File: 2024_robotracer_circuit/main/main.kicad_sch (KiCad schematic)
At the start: 71 parts, among them J1 PH_6p, J10 PH_5p, J11 PH_6p, J12 PH_4p, J13 PH_8p, J14 PH_6p, J2 Conn_02x05_Odd_Even, J3 Conn_02x05_Odd_Even, J4 PA_2p, J5 PA_2p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

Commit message: LEDつながた
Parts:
- removed J12: PH_4p, Connector_JST:JST_PH_B4B-PH-K_1x04_P2.00mm_Vertical, symbol Connector_Generic:Conn_01x04
- removed J14: PH_6p, Connector_JST:JST_PH_B6B-PH-K_1x06_P2.00mm_Vertical, symbol Connector_Generic:Conn_01x06
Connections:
- net ENC1_A: now also U1.37 (PC6); no longer U1.58 (PB6)
- net ENC1_B: now also U1.38 (PC7); no longer U1.59 (PB7)
- net ENC2_A: now also U1.58 (PB6); no longer U1.38 (PC7)
- net ENC2_B: now also U1.59 (PB7); no longer U1.37 (PC6)
- net LCD_SCL: now also J8.3 (Pin_3), R35.2; no longer J8.2 (Pin_2), R34.2
- net LCD_SDA: now also J8.2 (Pin_2), R34.2; no longer J8.3 (Pin_3), R35.2
- net LED0: now also U1.45 (PA12); no longer U1.8 (PC0)
- net LED1: now also U1.56 (PB4); no longer U1.9 (PC1)
- net LED2: now also U1.57 (PB5); no longer U1.2 (PC13)
- net LED3: now also U1.2 (PC13); no longer U1.3 (PC14)
- net LED4: now also U1.3 (PC14); no longer U1.4 (PC15)
- net LED5: now also U1.4 (PC15); no longer U1.33 (PB12)
- net LED6: now also U1.8 (PC0); no longer U1.57 (PB5)
- net LED7: now also U1.9 (PC1); no longer U1.56 (PB4)
- net LED9: now also U1.33 (PB12); no longer U1.45 (PA12)
- net MOTOR1_IN_A: now also U1.42 (PA9); no longer U1.41 (PA8)
- net MOTOR1_IN_B: now also U1.41 (PA8); no longer U1.42 (PA9)
- net MOTOR2_IN_A: now also U1.44 (PA11); no longer U1.43 (PA10)
- net MOTOR2_IN_B: now also U1.43 (PA10); no longer U1.44 (PA11)
- net SENSOR0_ADC: now also U1.17 (PA3); no longer U1.14 (PA0)
- net SENSOR1_ADC: now also U1.16 (PA2); no longer U1.15 (PA1)
- net SENSOR2_ADC: now also U1.15 (PA1); no longer U1.16 (PA2)
- net SENSOR3_ADC: now also U1.14 (PA0); no longer U1.17 (PA3)
- net SW_A: now also U1.24 (PC4); no longer U1.23 (PA7)
- net SW_B: now also U1.23 (PA7); no longer U1.24 (PC4)
- net SW_C: now also U1.27 (PB1); no longer U1.26 (PB0)
- net SW_D: now also U1.26 (PB0); no longer U1.27 (PB1)
- net PWM_GP: no longer names the net of U1.36 (PB15)
- net SPI_MISO_GP: no longer names the net of U1.10 (PC2)
- net SPI_MOSI_GP: no longer names the net of U1.11 (PC3)
- net SPI_SCK_GP: no longer names the net of U1.34 (PB13)
- net USART_RX: no longer names the net of U1.52 (PC11)
- net USART_TX: no longer names the net of U1.51 (PC10)
- no-connect marks 18 -> 24

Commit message: 修正
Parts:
- R23: value R_Small -> 1.8k
- R24: value R_Small -> 1k
- U3, U4: footprint Package_SO:TSSOP-8_3x3mm_P0.65mm -> Package_SO:SOP-8_3.9x4.9mm_P1.27mm
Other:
- moved on the sheet: BZ1, D1, J10, J11, J7, J9, R22, R23, R24, R5, R6, R7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

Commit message: hoge
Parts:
- J7: value HX_12p -> XH_12p
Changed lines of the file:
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@@
 			)
 		)
-		(property "Value" "HX_12p"
+		(property "Value" "XH_12p"
 			(at 59.69 154.9399 0)
 			(effects

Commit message: 修正
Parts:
- R31: value R_Small -> 5.1k
- R32: value R_Small -> 1.8k
- R33: value R_Small -> 3k
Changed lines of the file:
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@@
 			)
 		)
-		(property "Value" "R_Small"
+		(property "Value" "1.8k"
 			(at 179.07 41.9099 0)
 			(effects
@@
 			)
 		)
-		(property "Value" "R_Small"
+		(property "Value" "5.1k"
 			(at 90.17 39.3699 0)
 			(effects
@@
 			)
 		)
-		(property "Value" "R_Small"
+		(property "Value" "3k"
 			(at 175.26 73.6599 0)
 			(effects

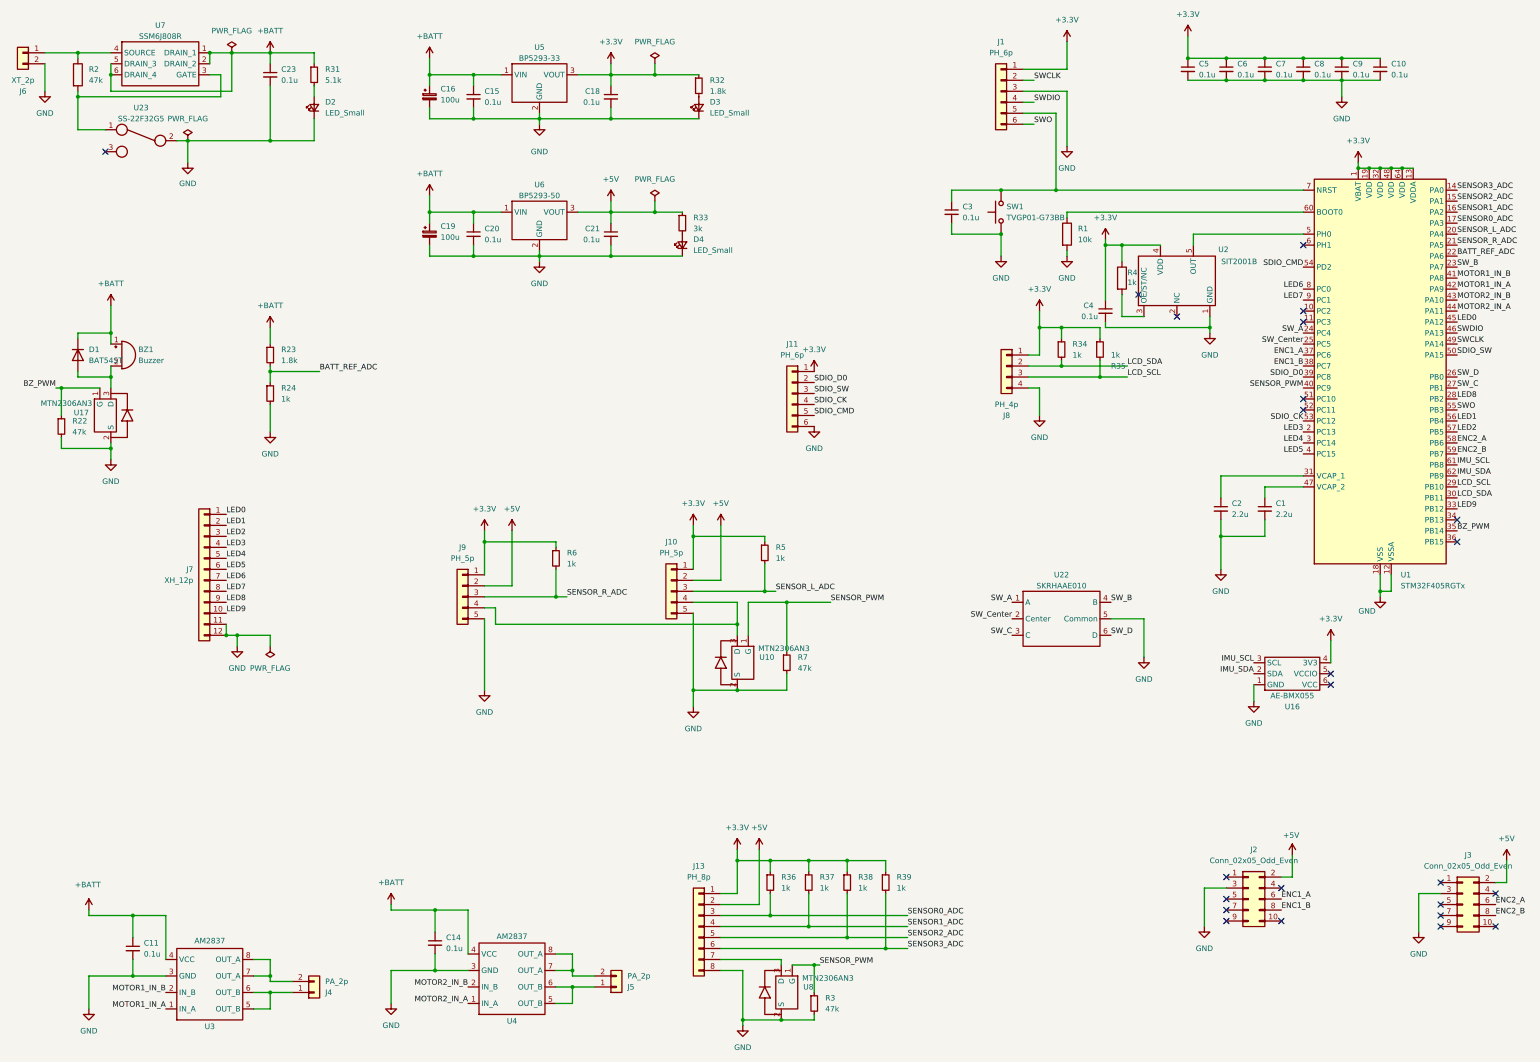
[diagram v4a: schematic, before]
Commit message: 回路を大幅修正
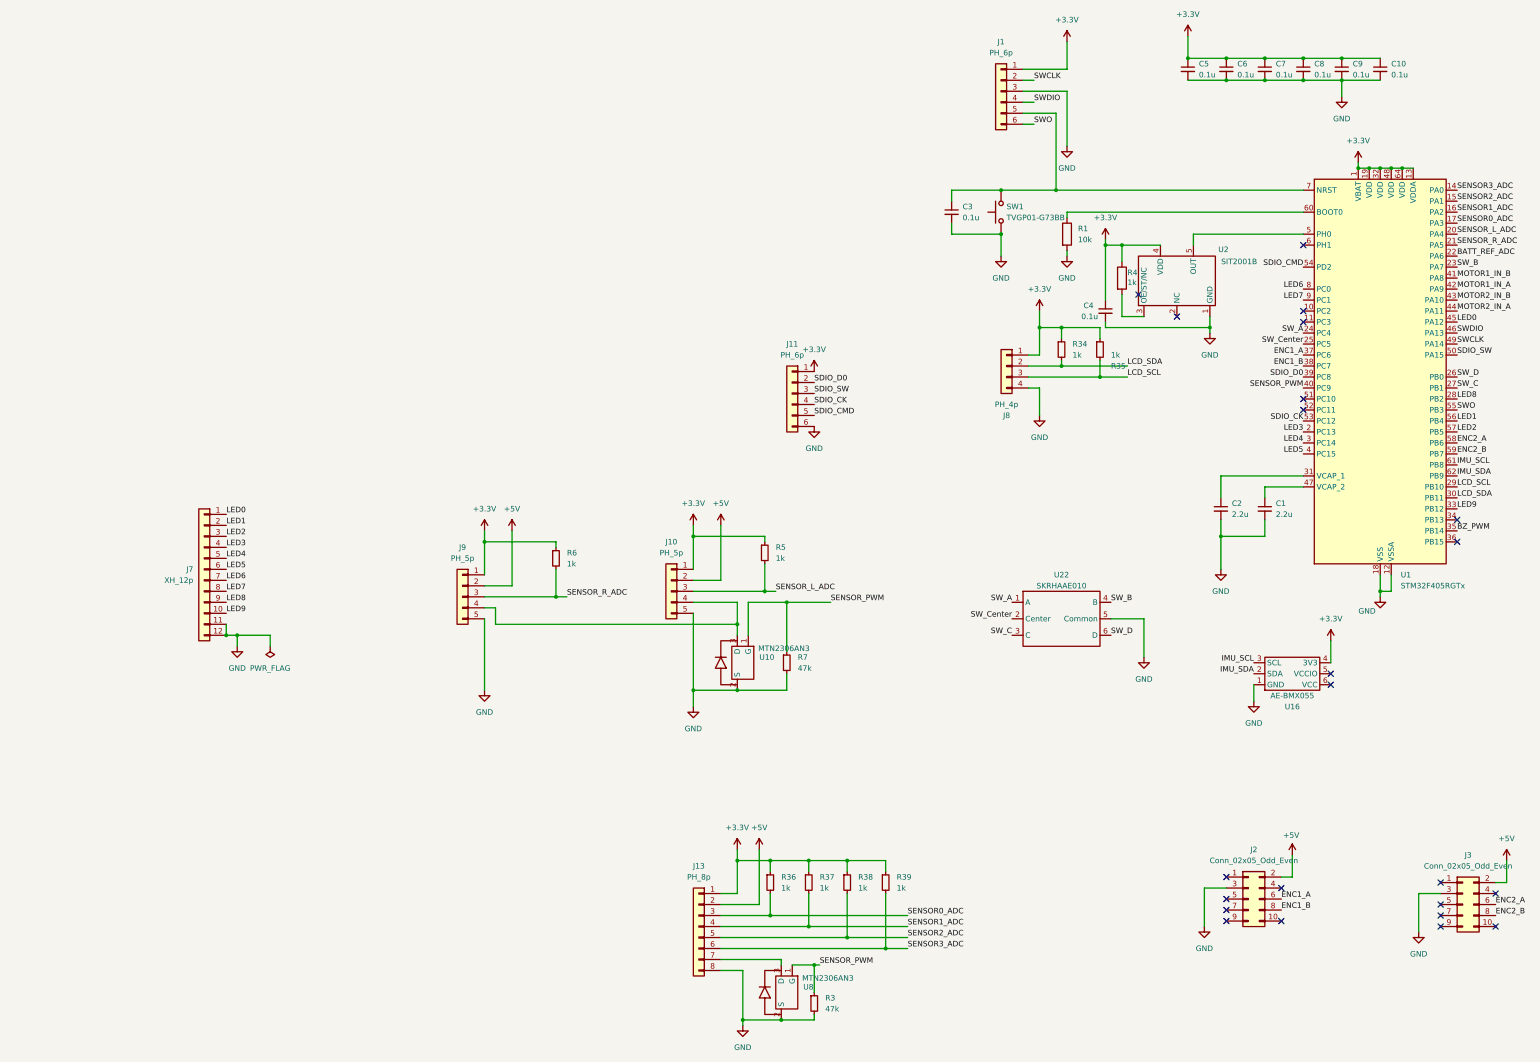
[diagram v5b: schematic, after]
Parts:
- removed BZ1: Buzzer, mylib:UM1515IA085008, symbol Device:Buzzer
- removed C11, C14, C15, C18, C20, C21, C23: 0.1u, Capacitor_SMD:C_0603_1608Metric_Pad1.08x0.95mm_HandSolder, symbol Device:C_Small
- removed C16, C19: 100u, Capacitor_SMD:CP_Elec_6.3x5.4, symbol Device:C_Polarized_Small
- removed D1: BAT54ST, Package_TO_SOT_SMD:SOT-523, symbol Device:D
- removed D2, D3, D4: LED_Small, LED_SMD:LED_0603_1608Metric_Pad1.05x0.95mm_HandSolder, symbol Device:LED_Small
- removed J4, J5: PA_2p, Connector_JST:JST_PH_B2B-PH-K_1x02_P2.00mm_Vertical, symbol Connector_Generic:Conn_01x02
- removed J6: XT_2p, Connector_AMASS:AMASS_XT30PW-M_1x02_P2.50mm_Horizontal, symbol Connector_Generic:Conn_01x02
- removed R2: 47k, Resistor_SMD:R_0603_1608Metric_Pad0.98x0.95mm_HandSolder, symbol Device:R
- removed R22: 47k, Resistor_SMD:R_0603_1608Metric_Pad0.98x0.95mm_HandSolder, symbol Device:R_Small
- removed R23, R32: 1.8k, Resistor_SMD:R_0603_1608Metric_Pad0.98x0.95mm_HandSolder, symbol Device:R_Small
- removed R24: 1k, Resistor_SMD:R_0603_1608Metric_Pad0.98x0.95mm_HandSolder, symbol Device:R_Small
- removed R31: 5.1k, Resistor_SMD:R_0603_1608Metric_Pad0.98x0.95mm_HandSolder, symbol Device:R_Small
- removed R33: 3k, Resistor_SMD:R_0603_1608Metric_Pad0.98x0.95mm_HandSolder, symbol Device:R_Small
- removed U17: MTN2306AN3, Package_TO_SOT_SMD:SOT-23, symbol mylib:MTN2306AN3
- removed U23: SS-22F32G5, Connector_PinHeader_2.54mm:PinHeader_1x03_P2.54mm_Vertical, symbol mylib:Toggle_SW
- removed U3, U4: AM2837, Package_SO:SOP-8_3.9x4.9mm_P1.27mm, symbol mylib:AM2837
- removed U5: BP5293-33, mylib:BP5293-xx, symbol mylib:BP5293-33
- removed U6: BP5293-50, mylib:BP5293-xx, symbol mylib:BP5293-50
- removed U7: SSM6J808R, Package_SO:TSOP-6_1.65x3.05mm_P0.95mm, symbol mylib:SSM6J808R
- U22: value SKRHAAE010 -> SKRHAAE010
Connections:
- no-connect marks 24 -> 23
